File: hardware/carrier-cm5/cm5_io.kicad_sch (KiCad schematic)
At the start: 55 parts, among them J1 Conn_02x02_Odd_Even, J14 FAN, J2 Conn_02x07_Odd_Even, J5 Conn_01x02, J6 THD-02-R, SW1 Right angle Tact button, U1 TPD4EUSB30, U18 RT9742GGJ5, U2 TPD4EUSB30, U3 MagJack-A70-112-331N126, U6 BS-0601-SK-4W

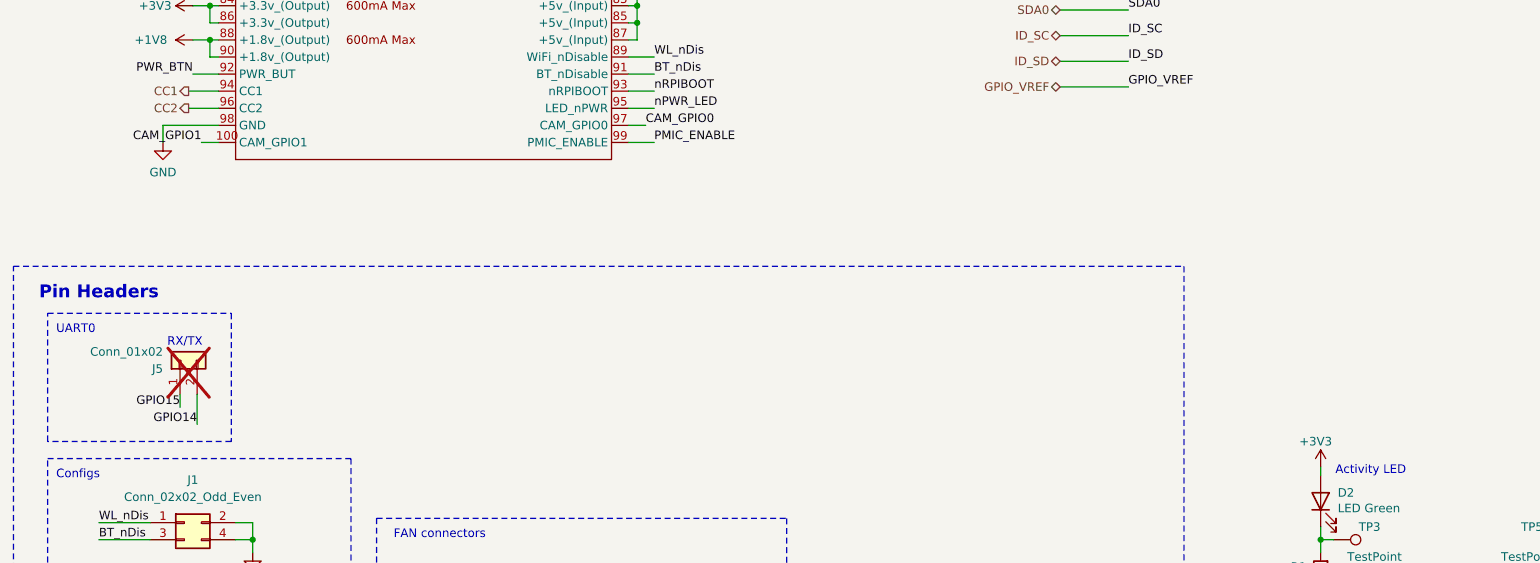
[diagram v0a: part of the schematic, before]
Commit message: cm5 carrier: console header, lidar connector, gpio allocation
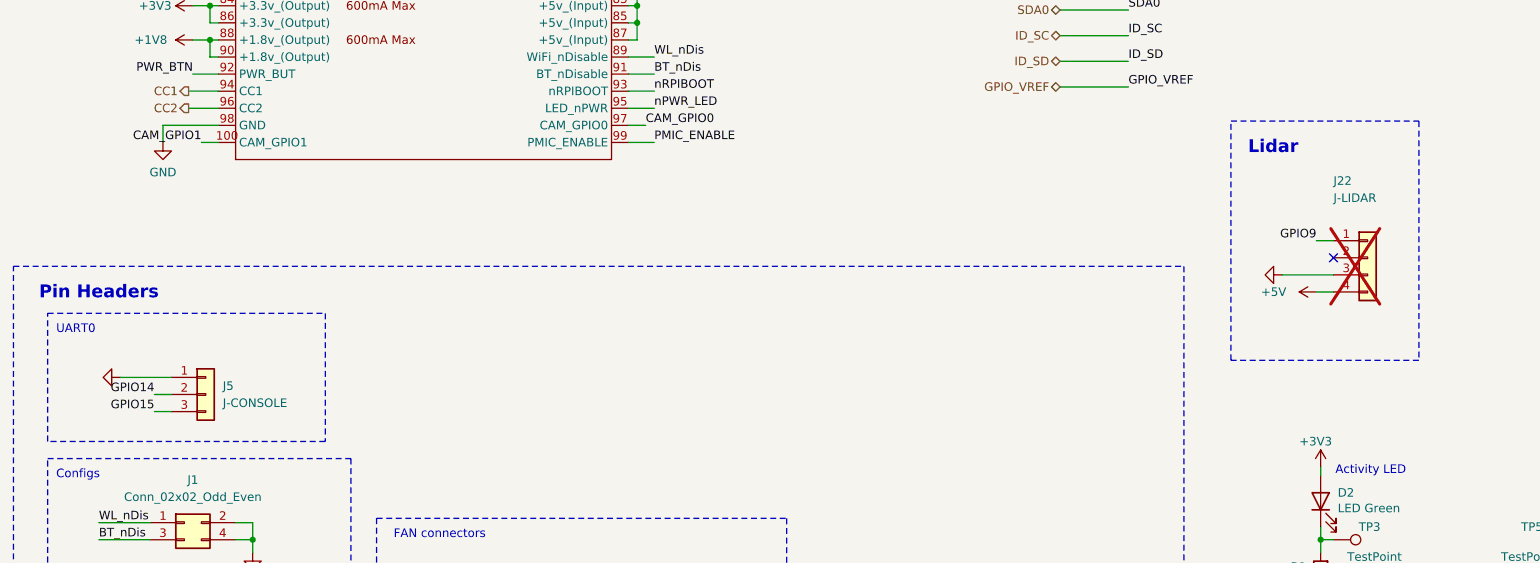
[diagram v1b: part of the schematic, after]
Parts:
- removed J5: Conn_01x02, Connector_PinHeader_2.54mm:PinHeader_1x02_P2.54mm_Vertical, symbol Connector_Generic:Conn_01x02
- added J22: J-LIDAR, Connector_JST:JST_GH_SM04B-GHS-TB_1x04-1MP_P1.25mm_Horizontal, symbol Connector_Generic:Conn_01x04
- added J5: J-CONSOLE, Connector_PinHeader_2.54mm:PinHeader_1x03_P2.54mm_Vertical, symbol Connector_Generic:Conn_01x03
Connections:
- net +5V: now also J22.4 (Pin_4)
- net GND: now also J22.3 (Pin_3), J5.1 (Pin_1)
- net GPIO14: now also J5.2 (Pin_2)
- net GPIO15: now also J5.3 (Pin_3)
- net GPIO9: now also J22.1 (Pin_1)
- no-connect marks 12 -> 13
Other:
- note added: "Lidar"
- note removed: "RX/TX"

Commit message: cm5 carrier: io mcu sheet (elrs, lidar, lora, adc, buzzer) and gnss sheet
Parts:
- removed J22: J-LIDAR, Connector_JST:JST_GH_SM04B-GHS-TB_1x04-1MP_P1.25mm_Horizontal, symbol Connector_Generic:Conn_01x04
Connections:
- net GPIO10 renamed SWDREC_SWDIO
- net GPIO11 renamed SWDREC_SWCLK
- net GPIO4 renamed IO_RXD
- net GPIO5 renamed IO_TXD
- net GPIO7 renamed GNSS_PPS
- net GPIO8 renamed SWDREC_NRST
- no-connect marks 13 -> 12
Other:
- note removed: "Lidar"

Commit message: cm5 carrier: a7670e lte sheet
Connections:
- net GPIO12 renamed LTE_TXD
- net GPIO13 renamed LTE_RXD
- net GPIO17 renamed LTE_PWRKEY
- net GPIO27 renamed LTE_SLEEP
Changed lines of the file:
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@@
 	(wire
 		(pts
-			(xy 368.3 226.06) (xy 368.3 231.14)
-		)
-		(stroke
-			(width 0)
-			(type default)
-		)
-	)
-	(wire
-		(pts
 			(xy 59.055 147.955) (xy 60.325 147.955)
 		)
@@
 		)
 	)
-	(label "GPIO13"
+	(label "LTE_RXD"
 		(at 56.515 71.755 180)
 		(effects
@@
 		)
 	)
-	(label "GPIO27"
+	(label "LTE_SLEEP"
 		(at 56.515 97.155 180)
 		(effects
@@
 		)
 	)
-	(label "GPIO12"
+	(label "LTE_TXD"
 		(at 125.095 76.835 0)
 		(effects
@@
 		)
 	)
-	(label "GPIO17"
+	(label "LTE_PWRKEY"
 		(at 56.515 99.695 180)
 		(effects
@@
 	)
 	(symbol
-		(lib_id "power:PWR_FLAG")
-		(at 368.3 226.06 0)
-		(unit 1)
-		(body_style 1)
-		(exclude_from_sim no)
-		(in_bom yes)
-		(on_board yes)
-		(in_pos_files yes)
-		(dnp no)
-		(property "Reference" "#FLG201"
-			(at 368.3 232.41 0)
-			(hide yes)
-			(show_name no)
-			(do_not_autoplace no)
-			(effects
-				(font
-					(size 1.27 1.27)
-				)
-			)
-		)
-		(property "Value" "PWR_FLAG"
-			(at 368.3 222.25 0)
-			(show_name no)
-			(do_not_autoplace no)
-			(effects
-				(font
-					(size 1.27 1.27)
-				)
-			)
-		)
-		(property "Footprint" ""
-			(at 368.3 226.06 0)
-			(show_name no)
-			(do_not_autoplace no)
-			(effects
-				(font
-					(size 1.27 1.27)
-				)
-			)
-		)
-		(property "Datasheet" ""
-			(at 368.3 226.06 0)
-			(show_name no)
-			(do_not_autoplace no)
-			(effects
-				(font
-					(size 1.27 1.27)
-				)
-			)
-		)
-		(property "Description" ""
-			(at 368.3 226.06 0)
-			(show_name no)
-			(do_not_autoplace no)
-			(effects
-				(font
-					(size 1.27 1.27)
-				)
-			)
-		)
-		(pin "1"
-		)
-		(instances
-			(project "carrier-cm5"
-				(path "/e63e39d7-6ac0-4ffd-8aa3-1841a4541b55/00000000-0000-0000-0000-00005cff706a"
-					(reference "#FLG201")
-					(unit 1)
-				)
-			)
-		)
-	)
-	(symbol
 		(lib_id "power:+3V3")
 		(at 56.515 142.875 90)
@@
 	)
 	(symbol
-		(lib_id "power:+3V3")
-		(at 368.3 231.14 180)
-		(unit 1)
-		(body_style 1)
-		(exclude_from_sim no)
-		(in_bom yes)
-		(on_board yes)
-		(in_pos_files yes)
-		(dnp no)
-		(property "Reference" "#PWR311"
-			(at 368.3 237.49 0)
-			(hide yes)
-			(show_name no)
-			(do_not_autoplace no)
-			(effects
-				(font
-					(size 1.27 1.27)
-				)
-			)
-		)
-		(property "Value" "+3V3"
-			(at 368.3 234.95 0)
-			(show_name no)
-			(do_not_autoplace no)
-			(effects
-				(font
-					(size 1.27 1.27)
-				)
-			)
-		)
-		(property "Footprint" ""
-			(at 368.3 231.14 0)
-			(show_name no)
-			(do_not_autoplace no)
-			(effects
-				(font
-					(size 1.27 1.27)
-				)
-			)
-		)
-		(property "Datasheet" ""
-			(at 368.3 231.14 0)
-			(show_name no)
-			(do_not_autoplace no)
-			(effects
-				(font
-					(size 1.27 1.27)
-				)
-			)
-		)
-		(property "Description" ""
-			(at 368.3 231.14 0)
-			(show_name no)
-			(do_not_autoplace no)
-			(effects
-				(font
-					(size 1.27 1.27)
-				)
-			)
-		)
-		(pin "1"
-		)
-		(instances
-			(project "carrier-cm5"
-				(path "/e63e39d7-6ac0-4ffd-8aa3-1841a4541b55/00000000-0000-0000-0000-00005cff706a"
-					(reference "#PWR311")
-					(unit 1)
-				)
-			)
-		)
-	)
-	(symbol
 		(lib_id "power:PWR_FLAG")
 		(at 381 226.06 0)
@@
 		(fields_autoplaced yes)
 		(effects
+			(font
+				(size 1.27 1.27)
+			)
+			(justify left bottom)
+		)
+	)
+	(hierarchical_label "LTE_TXD"
+		(shape bidirectional)
+		(at 215.9 187.96 180)
+		(fields_autoplaced yes)
+		(effects
+			(font
+				(size 1.27 1.27)
+			)
+			(justify right)
+		)
+	)
+	(wire
+		(pts
+			(xy 215.9 187.96) (xy 226.06 187.96)
+		)
+		(stroke
+			(width 0)
+			(type default)
+		)
+	)
+	(label "LTE_TXD"
+		(at 226.06 187.96 0)
+		(fields_autoplaced yes)
+		(effects
+			(font
+				(size 1.27 1.27)
+			)
+			(justify left bottom)
+		)
+	)
+	(hierarchical_label "LTE_RXD"
+		(shape bidirectional)
+		(at 215.9 191.77 180)
+		(fields_autoplaced yes)
+		(effects
+			(font
+				(size 1.27 1.27)
+			)
+			(justify right)
+		)
+	)
+	(wire
+		(pts
+			(xy 215.9 191.77) (xy 226.06 191.77)
+		)
+		(stroke
+			(width 0)
+			(type default)
+		)
+	)
+	(label "LTE_RXD"
+		(at 226.06 191.77 0)
+		(fields_autoplaced yes)
+		(effects
+			(font
+				(size 1.27 1.27)
+			)
+			(justify left bottom)
+		)
+	)
+	(hierarchical_label "LTE_PWRKEY"
+		(shape bidirectional)
+		(at 215.9 195.58 180)
+		(fields_autoplaced yes)
+		(effects
+			(font
+				(size 1.27 1.27)
+			)
+			(justify right)
+		)
+	)
+	(wire
+		(pts
+			(xy 215.9 195.58) (xy 226.06 195.58)
+		)
+		(stroke
+			(width 0)
+			(type default)
+		)
+	)
+	(label "LTE_PWRKEY"
+		(at 226.06 195.58 0)
+		(fields_autoplaced yes)
+		(effects
+			(font
+				(size 1.27 1.27)
+			)
+			(justify left bottom)
+		)
+	)
+	(hierarchical_label "LTE_SLEEP"
+		(shape bidirectional)
+		(at 215.9 199.39 180)
+		(fields_autoplaced yes)
+		(effects
+			(font
+				(size 1.27 1.27)
+			)
+			(justify right)
+		)
+	)
+	(wire
+		(pts
+			(xy 215.9 199.39) (xy 226.06 199.39)
+		)
+		(stroke
+			(width 0)
+			(type default)
+		)
+	)
+	(label "LTE_SLEEP"
+		(at 226.06 199.39 0)
+		(fields_autoplaced yes)
+		(effects

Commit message: cm5 carrier: can, imu, j-nose, swd recovery, j-sysctl gpios
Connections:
- net GPIO16 renamed CAN_INT
- net GPIO18 renamed CAN_CS
- net GPIO19 renamed CAN_MISO
- net GPIO2 renamed I2C1_SDA
- net GPIO20 renamed CAN_MOSI
- net GPIO21 renamed CAN_SCK
- net GPIO22 renamed SHUTDOWN_REQ_N
- net GPIO23 renamed HALTED
- net GPIO24 renamed ESTOP_N
- net GPIO25 renamed TOF_INT
- net GPIO26 renamed TOF_LPN
- net GPIO3 renamed I2C1_SCL
- net GPIO6 renamed IMU_INT
- net GPIO9 renamed MAG_INT

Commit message: Updated schematic on CM5 carrier
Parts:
- D301: renamed from D2; value LED Green -> Green
- D302: renamed from D1; value LED Red -> Red
- renumbered C1 to C301, C5 to C302, Card1 to Card301, J2 to J301, J1 to J302, J5 to J303, J6 to J304, J14 to J305, Module1 to Module201, R6 to R301, R11 to R302, R7 to R303, R1 to R304, R10 to R305, R2 to R306, R3 to R307, R13 to R308, R5 to R309, R4 to R310, SW1 to SW301, TP2 to TP301, TP4 to TP302, TP12 to TP303, TP13 to TP304, TP15 to TP305, TP18 to TP306, TP21 to TP307, TP24 to TP308, TP27 to TP309, TP16 to TP310, TP19 to TP311, TP22 to TP312, TP25 to TP313, TP28 to TP314, TP17 to TP315, TP20 to TP316, TP23 to TP317, TP26 to TP318, TP29 to TP319, TP3 to TP320, TP5 to TP321, TP1 to TP322, TP6 to TP323, TP7 to TP324, TP8 to TP325, TP9 to TP326, TP10 to TP327, TP11 to TP328, U6 to U301, U2 to U302, U1 to U303, U18 to U304, U3 to U305
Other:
- moved on the sheet: D301, D302, J304, J305, R301, R302, R303, R304, R305, R309, R310, SW301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
